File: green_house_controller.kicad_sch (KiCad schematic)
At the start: 9 parts

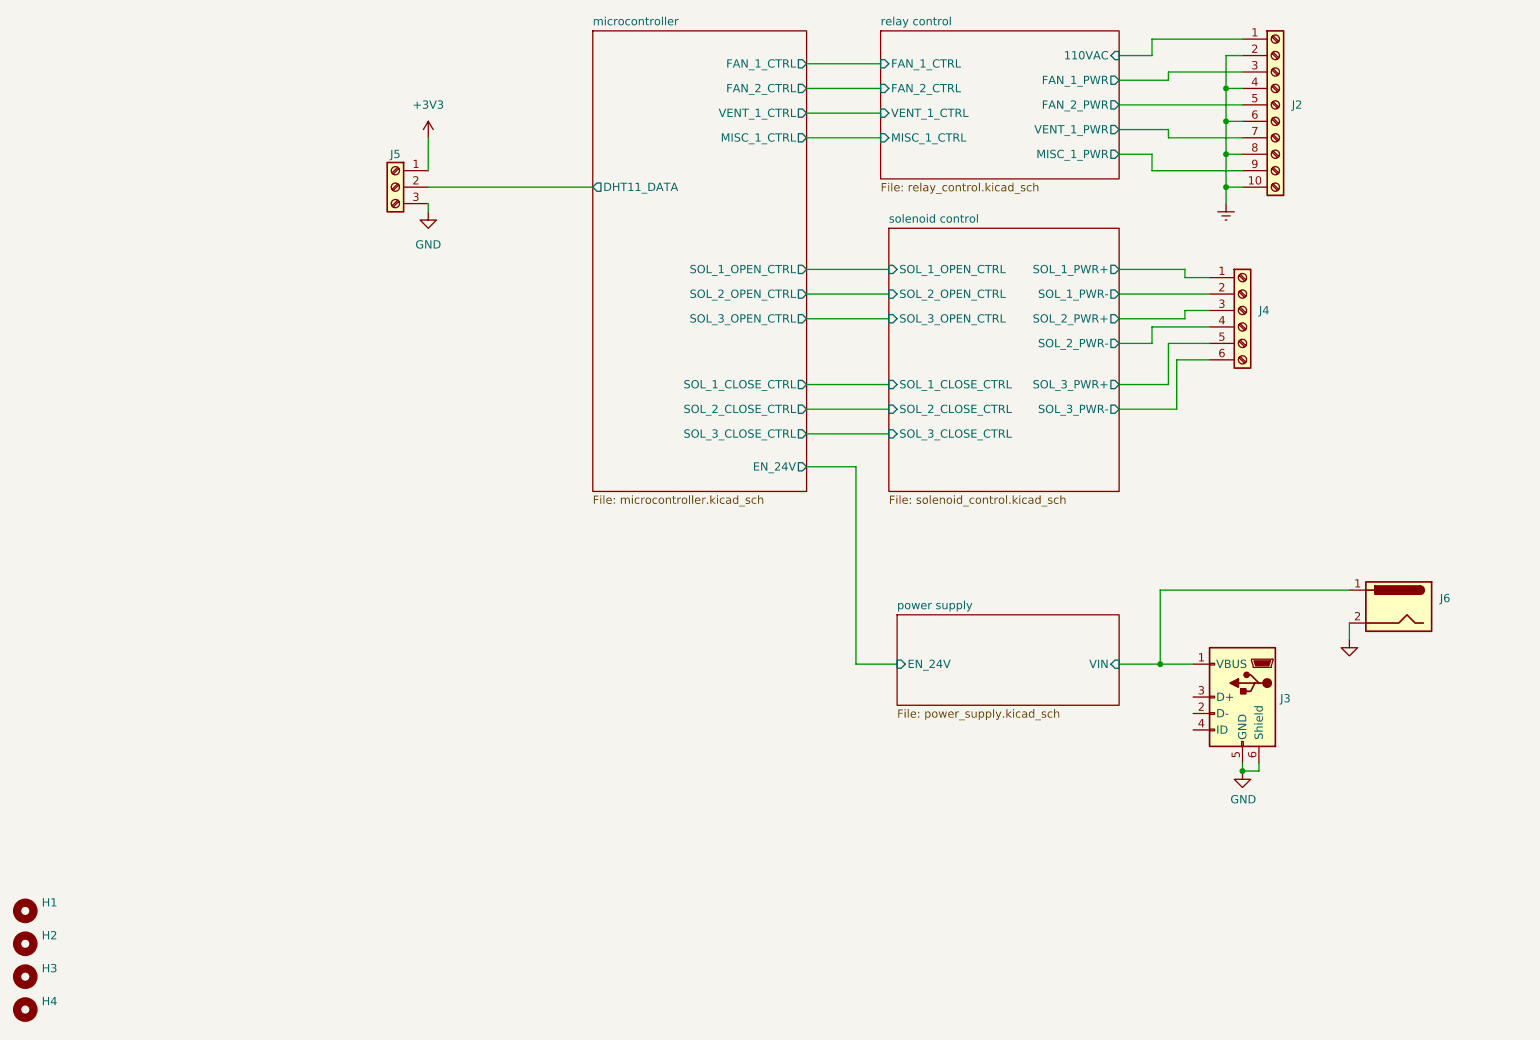
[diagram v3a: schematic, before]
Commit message: Finished initial layout.  Zero DRC errors/warnings.
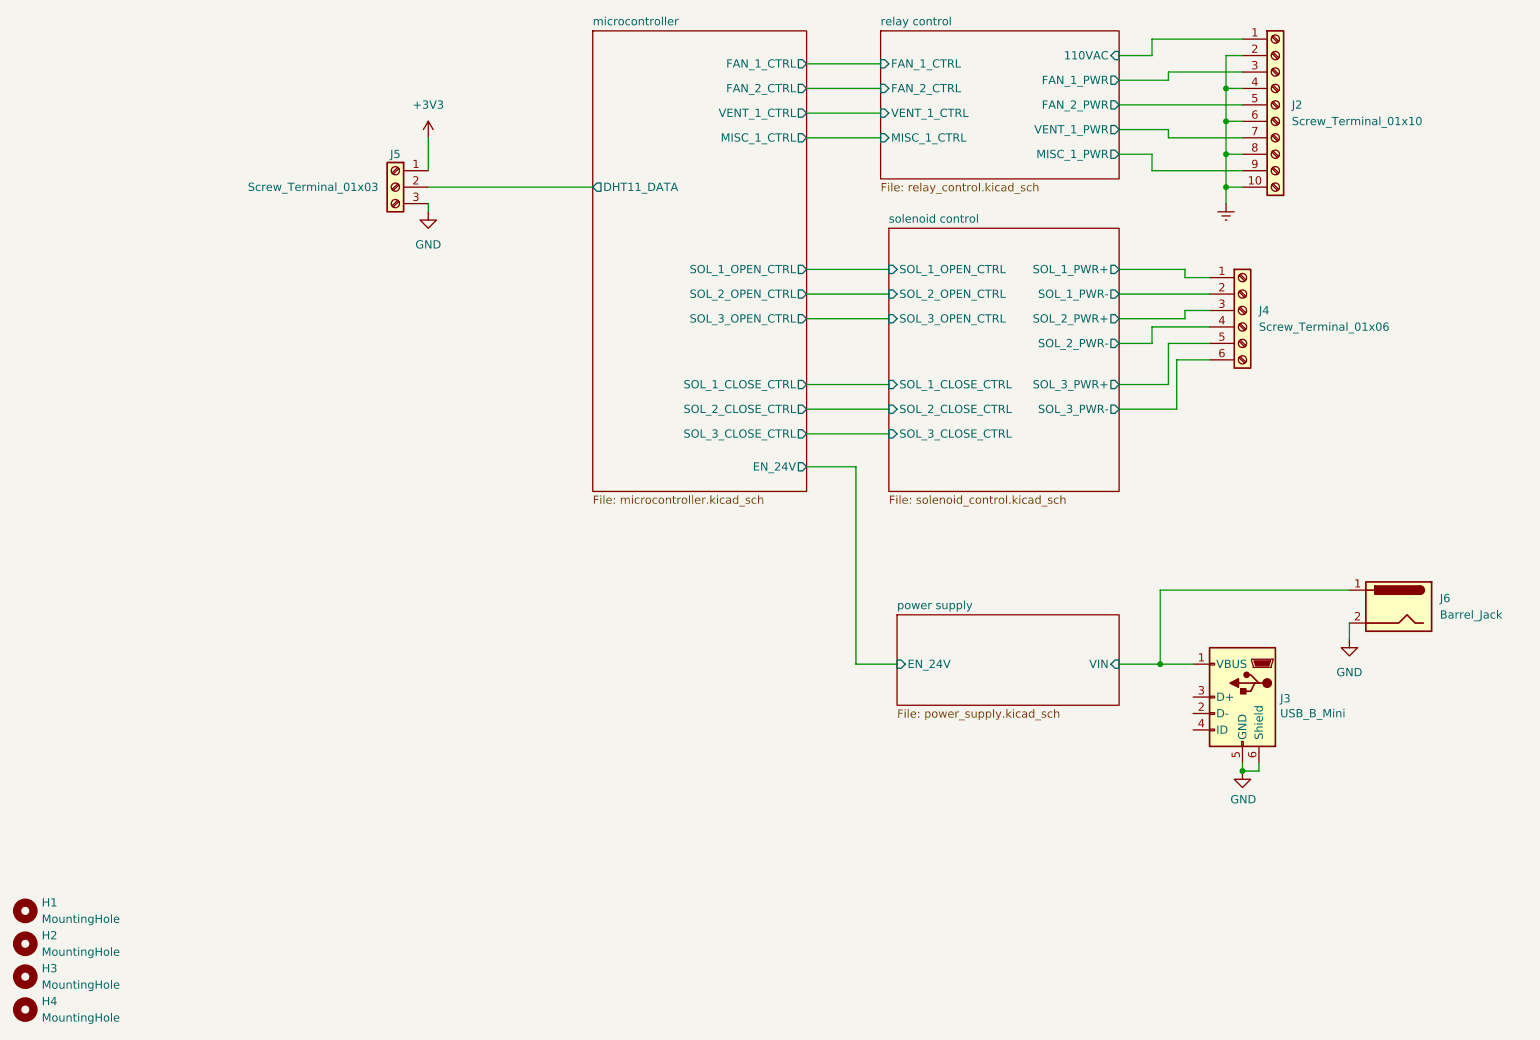
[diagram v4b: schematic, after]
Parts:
- H1, H2, H3, H4: value (none) -> MountingHole; footprint (none) -> MountingHole:MountingHole_3.2mm_M3
- J2: value (none) -> Screw_Terminal_01x10; footprint (none) -> Connector_Phoenix_MC_HighVoltage:PhoenixContact_MCV_1,5_10-G-5.08_1x10_P5.08mm_Vertical
- J3: value (none) -> USB_B_Mini; footprint (none) -> Connector_USB:USB_Mini-B_Lumberg_2486_01_Horizontal
- J4: value (none) -> Screw_Terminal_01x06; footprint (none) -> Connector_Phoenix_MC_HighVoltage:PhoenixContact_MCV_1,5_6-G-5.08_1x06_P5.08mm_Vertical
- J5: value (none) -> Screw_Terminal_01x03; footprint (none) -> Connector_Phoenix_MC_HighVoltage:PhoenixContact_MCV_1,5_3-G-5.08_1x03_P5.08mm_Vertical
- J6: value (none) -> Barrel_Jack; footprint (none) -> Connector_BarrelJack:BarrelJack_CUI_PJ-102AH_Horizontal
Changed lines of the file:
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@@
       (effects (font (size 1.27 1.27)) (justify right))
     )
-    (property "Value" "" (id 1) (at 212.8266 147.32 0)
-      (effects (font (size 1.27 1.27)) (justify right))
-    )
-    (property "Footprint" "" (id 2) (at 203.2 146.05 0)
+    (property "Value" "USB_B_Mini" (id 1) (at 212.8266 147.32 0)
+      (effects (font (size 1.27 1.27)) (justify right))
+    )
+    (property "Footprint" "Connector_USB:USB_Mini-B_Lumberg_2486_01_Horizontal" (id 2) (at 203.2 146.05 0)
       (effects (font (size 1.27 1.27)) hide)
     )
@@
       (effects (font (size 1.27 1.27)) (justify left))
     )
-    (property "Value" "" (id 1) (at 214.63 55.8799 0)
-      (effects (font (size 1.27 1.27)) (justify left))
-    )
-    (property "Footprint" "" (id 2) (at 212.09 53.34 0)
+    (property "Value" "Screw_Terminal_01x10" (id 1) (at 214.63 55.8799 0)
+      (effects (font (size 1.27 1.27)) (justify left))
+    )
+    (property "Footprint" "Connector_Phoenix_MC_HighVoltage:PhoenixContact_MCV_1,5_10-G-5.08_1x10_P5.08mm_Vertical" (id 2) (at 212.09 53.34 0)
       (effects (font (size 1.27 1.27)) hide)
     )
@@
       (effects (font (size 1.27 1.27)) (justify left))
     )
-    (property "Value" "" (id 1) (at 21.59 194.3099 0)
-      (effects (font (size 1.27 1.27)) (justify left))
-    )
-    (property "Footprint" "" (id 2) (at 19.05 193.04 0)
+    (property "Value" "MountingHole" (id 1) (at 21.59 194.3099 0)
+      (effects (font (size 1.27 1.27)) (justify left))
+    )
+    (property "Footprint" "MountingHole:MountingHole_3.2mm_M3" (id 2) (at 19.05 193.04 0)
       (effects (font (size 1.27 1.27)) hide)
     )
@@
       (effects (font (size 1.27 1.27)) (justify right))
     )
-    (property "Value" "" (id 1) (at 237.49 132.0799 0)
-      (effects (font (size 1.27 1.27)) (justify right))
-    )
-    (property "Footprint" "" (id 2) (at 229.87 131.826 0)
+    (property "Value" "Barrel_Jack" (id 1) (at 237.49 132.0799 0)
+      (effects (font (size 1.27 1.27)) (justify right))
+    )
+    (property "Footprint" "Connector_BarrelJack:BarrelJack_CUI_PJ-102AH_Horizontal" (id 2) (at 229.87 131.826 0)
       (effects (font (size 1.27 1.27)) hide)
     )
@@
       (effects (font (size 1.27 1.27)) (justify left))
     )
-    (property "Value" "" (id 1) (at 21.59 184.1499 0)
-      (effects (font (size 1.27 1.27)) (justify left))
-    )
-    (property "Footprint" "" (id 2) (at 19.05 182.88 0)
+    (property "Value" "MountingHole" (id 1) (at 21.59 184.1499 0)
+      (effects (font (size 1.27 1.27)) (justify left))
+    )
+    (property "Footprint" "MountingHole:MountingHole_3.2mm_M3" (id 2) (at 19.05 182.88 0)
       (effects (font (size 1.27 1.27)) hide)
     )
@@
       (effects (font (size 1.27 1.27)) hide)
     )
-    (property "Value" "" (id 1) (at 204.47 72.39 0)
+    (property "Value" "Earth" (id 1) (at 204.47 72.39 0)
       (effects (font (size 1.27 1.27)) hide)
     )
@@
       (effects (font (size 1.27 1.27)) (justify left))
     )
-    (property "Value" "" (id 1) (at 21.59 179.0699 0)
-      (effects (font (size 1.27 1.27)) (justify left))
-    )
-    (property "Footprint" "" (id 2) (at 19.05 177.8 0)
+    (property "Value" "MountingHole" (id 1) (at 21.59 179.0699 0)
+      (effects (font (size 1.27 1.27)) (justify left))
+    )
+    (property "Footprint" "MountingHole:MountingHole_3.2mm_M3" (id 2) (at 19.05 177.8 0)
       (effects (font (size 1.27 1.27)) hide)
     )
@@
       (effects (font (size 1.27 1.27)) (justify left))
     )
-    (property "Value" "" (id 1) (at 209.55 87.6299 0)
-      (effects (font (size 1.27 1.27)) (justify left))
-    )
-    (property "Footprint" "" (id 2) (at 207.01 85.09 0)
+    (property "Value" "Screw_Terminal_01x06" (id 1) (at 209.55 87.6299 0)
+      (effects (font (size 1.27 1.27)) (justify left))
+    )
+    (property "Footprint" "Connector_Phoenix_MC_HighVoltage:PhoenixContact_MCV_1,5_6-G-5.08_1x06_P5.08mm_Vertical" (id 2) (at 207.01 85.09 0)
       (effects (font (size 1.27 1.27)) hide)
     )
@@
     (in_bom yes) (on_board yes)
     (property "Reference" "J5" (id 0) (at 76.2 60.96 0))
-    (property "Value" "" (id 1) (at 63.5 66.04 0))
-    (property "Footprint" "" (id 2) (at 76.2 66.04 0)
+    (property "Value" "Screw_Terminal_01x03" (id 1) (at 63.5 66.04 0))
+    (property "Footprint" "Connector_Phoenix_MC_HighVoltage:PhoenixContact_MCV_1,5_3-G-5.08_1x03_P5.08mm_Vertical" (id 2) (at 76.2 66.04 0)
       (effects (font (size 1.27 1.27)) hide)
     )
@@
       (effects (font (size 1.27 1.27)) hide)
     )
-    (property "Value" "" (id 1) (at 223.52 140.97 0))
+    (property "Value" "GND" (id 1) (at 223.52 140.97 0))
     (property "Footprint" "" (id 2) (at 223.52 135.89 0)
       (effects (font (size 1.27 1.27)) hide)
@@
       (effects (font (size 1.27 1.27)) (justify left))
     )
-    (property "Value" "" (id 1) (at 21.59 189.2299 0)
-      (effects (font (size 1.27 1.27)) (justify left))
-    )
-    (property "Footprint" "" (id 2) (at 19.05 187.96 0)
-      (effects (font (size 1.27 1.27)) hide)
-    )
+    (property "Value" "MountingHole" (id 1) (at 21.59 189.2299 0)
+      (effects (font (size 1.27 1.27)) (justify left))
+    )
+    (property "Footprint" "MountingHole:MountingHole_3.2mm_M3" (id 2) (at 19.05 187.96 0)
+      (effects (font (size 1.27 1.27)) hide)
+    )

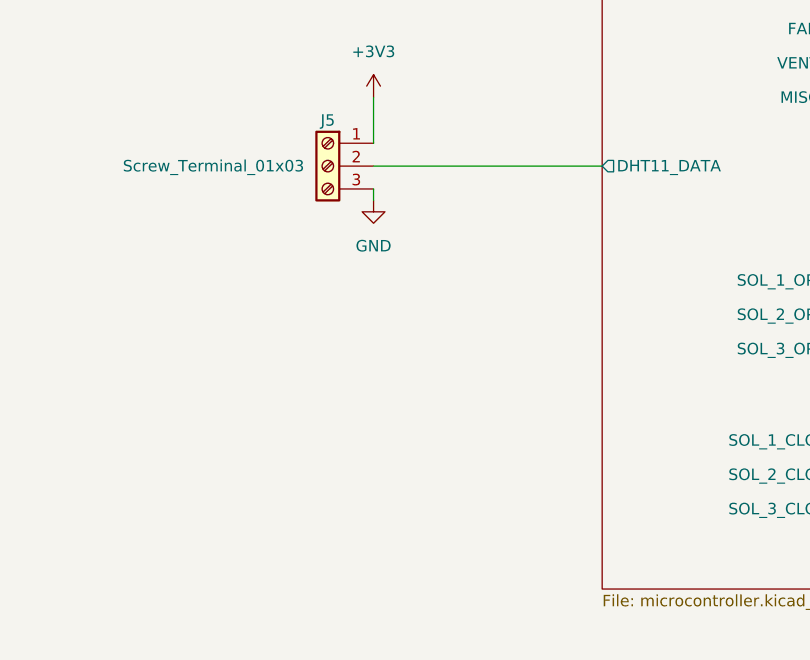
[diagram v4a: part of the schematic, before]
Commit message: Added DHT11 footprint. Updated feedback resistor values for regulator circuit. Created gerber and drill files for version 1.
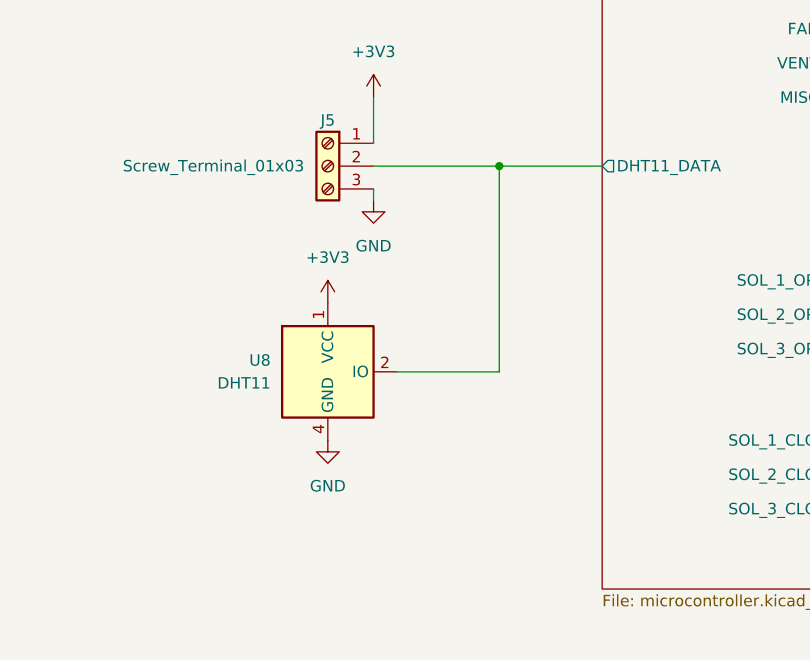
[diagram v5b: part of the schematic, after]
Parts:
- added U8: DHT11, Sensor:Aosong_DHT11_5.5x12.0_P2.54mm, symbol Sensor:DHT11
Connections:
- net +3V3: now also U8.1 (VCC)
- net GND: now also U8.4 (GND)
- net microcontroller/DHT11_DATA: now also U8.2 (IO)
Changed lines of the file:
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@@
   (junction (at 194.31 139.7) (diameter 0) (color 0 0 0 0)
   )
+  (junction (at 95.25 66.04) (diameter 0) (color 0 0 0 0)
+  )
   (junction (at 204.47 55.88) (diameter 0) (color 0 0 0 0)
   )
@@
     (stroke (width 0) (type default) (color 0 0 0 0))
   )
-  (wire (pts (xy 81.28 66.04) (xy 106.68 66.04))
+  (wire (pts (xy 81.28 66.04) (xy 95.25 66.04))
     (stroke (width 0) (type default) (color 0 0 0 0))
   )
@@
     (stroke (width 0) (type default) (color 0 0 0 0))
   )
+  (wire (pts (xy 95.25 66.04) (xy 106.68 66.04))
+    (stroke (width 0) (type default) (color 0 0 0 0))
+  )
   (wire (pts (xy 139.7 54.61) (xy 151.13 54.61))
     (stroke (width 0) (type default) (color 0 0 0 0))
@@
     (stroke (width 0) (type default) (color 0 0 0 0))
   )
+  (wire (pts (xy 83.82 88.9) (xy 95.25 88.9))
+    (stroke (width 0) (type default) (color 0 0 0 0))
+  )
   (wire (pts (xy 139.7 86.36) (xy 152.4 86.36))
     (stroke (width 0) (type default) (color 0 0 0 0))
@@
   )
   (wire (pts (xy 187.96 60.96) (xy 193.04 60.96))
+    (stroke (width 0) (type default) (color 0 0 0 0))
+  )
+  (wire (pts (xy 95.25 88.9) (xy 95.25 66.04))
     (stroke (width 0) (type default) (color 0 0 0 0))
   )
@@
     (pin "1")
   )
+  (symbol (lib_id "power:GND") (at 76.2 96.52 0) (unit 1)
+    (in_bom yes) (on_board yes) (fields_autoplaced)
+    (property "Reference" "#PWR039" (id 0) (at 76.2 102.87 0)
+      (effects (font (size 1.27 1.27)) hide)
+    )
+    (property "Value" "GND" (id 1) (at 76.2 101.6 0))
+    (property "Footprint" "" (id 2) (at 76.2 96.52 0)
+      (effects (font (size 1.27 1.27)) hide)
+    )
+    (property "Datasheet" "" (id 3) (at 76.2 96.52 0)
+      (effects (font (size 1.27 1.27)) hide)
+    )
+    (pin "1")
+  )
   (symbol (lib_id "Connector:Barrel_Jack") (at 231.14 130.81 0) (mirror y) (unit 1)
     (in_bom yes) (on_board yes) (fields_autoplaced)
@@
     )
   )
+  (symbol (lib_id "Sensor:DHT11") (at 76.2 88.9 0) (unit 1)
+    (in_bom yes) (on_board yes) (fields_autoplaced)
+    (property "Reference" "U8" (id 0) (at 69.85 87.6299 0)
+      (effects (font (size 1.27 1.27)) (justify right))
+    )
+    (property "Value" "DHT11" (id 1) (at 69.85 90.1699 0)
+      (effects (font (size 1.27 1.27)) (justify right))
+    )
+    (property "Footprint" "Sensor:Aosong_DHT11_5.5x12.0_P2.54mm" (id 2) (at 76.2 99.06 0)
+      (effects (font (size 1.27 1.27)) hide)
+    )
+    (property "Datasheet" "http://akizukidenshi.com/download/ds/aosong/DHT11.pdf" (id 3) (at 80.01 82.55 0)
+      (effects (font (size 1.27 1.27)) hide)
+    )
+    (pin "1")
+    (pin "2")
+    (pin "3")
+    (pin "4")
+  )
   (symbol (lib_id "power:+3V3") (at 81.28 58.42 0) (unit 1)
     (in_bom yes) (on_board yes) (fields_autoplaced)
@@
     )
     (property "Datasheet" "" (id 3) (at 81.28 58.42 0)
+      (effects (font (size 1.27 1.27)) hide)
+    )
+    (pin "1")
+  )
+  (symbol (lib_id "power:+3V3") (at 76.2 81.28 0) (unit 1)
+    (in_bom yes) (on_board yes) (fields_autoplaced)
+    (property "Reference" "#PWR037" (id 0) (at 76.2 85.09 0)
+      (effects (font (size 1.27 1.27)) hide)
+    )
+    (property "Value" "+3V3" (id 1) (at 76.2 76.2 0))
+    (property "Footprint" "" (id 2) (at 76.2 81.28 0)
+      (effects (font (size 1.27 1.27)) hide)
+    )
+    (property "Datasheet" "" (id 3) (at 76.2 81.28 0)
       (effects (font (size 1.27 1.27)) hide)
     )
@@
       (reference "#PWR036") (unit 1) (value "GND") (footprint "")
     )
+    (path "/a4a197a0-c5de-4c84-b501-b5fb434885cb"
+      (reference "#PWR037") (unit 1) (value "+3V3") (footprint "")
+    )
     (path "/404cdc0e-3364-48be-934e-b6ed8f40ff27/1ee8f5ae-fa9b-4704-a66d-8f1da92d3867"
       (reference "#PWR038") (unit 1) (value "GND") (footprint "")
     )
+    (path "/604d893e-380a-42df-9481-6724dc67b540"
+      (reference "#PWR039") (unit 1) (value "GND") (footprint "")
+    )
     (path "/404cdc0e-3364-48be-934e-b6ed8f40ff27/25550c90-c85d-4620-8b36-b4ee21db966b"
       (reference "#PWR040") (unit 1) (value "GND") (footprint "")
@@
     )
     (path "/00000000-0000-0000-0000-0000625b57c4/00000000-0000-0000-0000-000062633f01"
-      (reference "R11") (unit 1) (value "150K") (footprint "Resistor_SMD:R_0805_2012Metric")
+      (reference "R11") (unit 1) (value "22K") (footprint "Resistor_SMD:R_0805_2012Metric")
     )
     (path "/00000000-0000-0000-0000-0000625b57c4/00000000-0000-0000-0000-000062633f79"
-      (reference "R12") (unit 1) (value "5.36K") (footprint "Resistor_SMD:R_0805_2012Metric")
+      (reference "R12") (unit 1) (value "10K") (footprint "Resistor_SMD:R_0805_2012Metric")
     )
     (path "/00000000-0000-0000-0000-0000625b57c4/00000000-0000-0000-0000-0000626361e5"
@@
     )
     (path "/00000000-0000-0000-0000-0000625b57c4/ed839c10-345c-4341-951a-9b22a02fff73"
-      (reference "R37") (unit 1) (value "1K") (footprint "Resistor_SMD:R_0805_2012Metric")
+      (reference "R37") (unit 1) (value "18.7K") (footprint "Resistor_SMD:R_0805_2012Metric")
     )
     (path "/404cdc0e-3364-48be-934e-b6ed8f40ff27/a1119f67-8f92-4a25-a4f7-5f69d2398d9a"
@@
       (reference "U7") (unit 1) (value "LM2733XMF") (footprint "Package_TO_SOT_SMD:SOT-23-5")
     )
-  )
+    (path "/9fd3118a-c77c-42db-b932-4ceeaba9dbcc"
+      (reference "U8") (unit 1) (value "DHT11") (footprint "Sensor:Aosong_DHT11_5.5x12.0_P2.54mm")
+    )
+  )
